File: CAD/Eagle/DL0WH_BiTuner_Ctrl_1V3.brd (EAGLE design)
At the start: 96.5 x 73 mm, 157 parts, among them Q0321 ABS07-32.768KHZ, U0101 STM32L476RGT6_64PIN_LDO, U0601 MC33996, U0701 MC33996, U0801 MC33996, U0921 TS5A23166, U0941 LM2611, U0951 OPA354, U0961 OPA354, U0962 MCP4661-103E-MS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

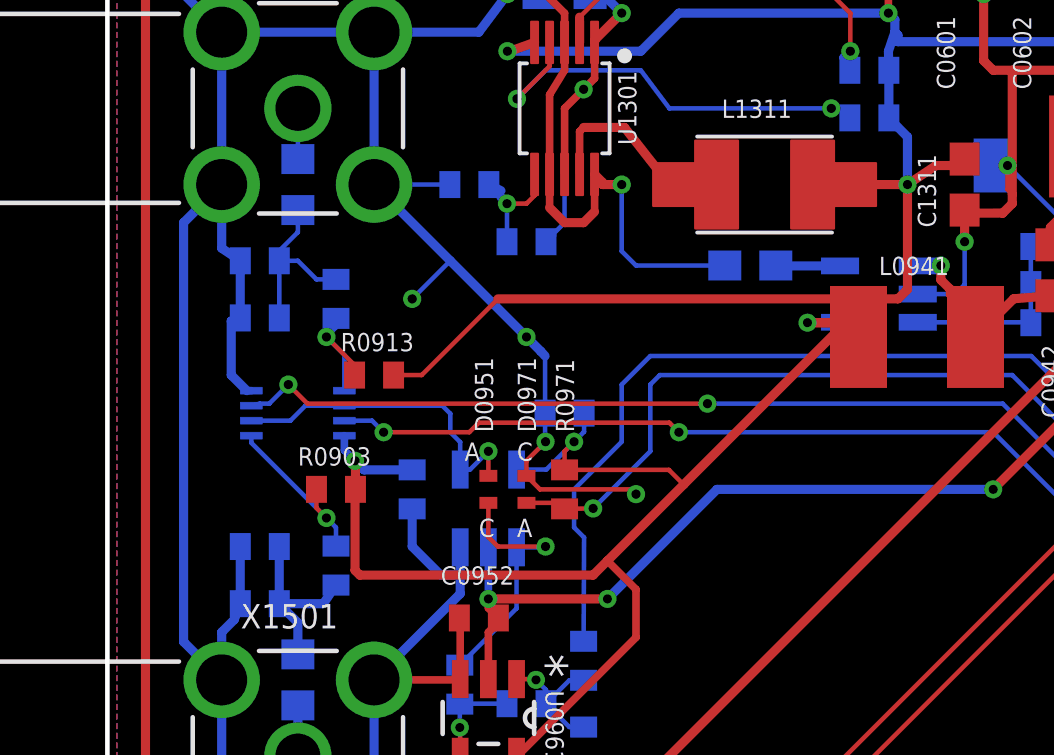
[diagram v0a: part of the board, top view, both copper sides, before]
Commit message: HW_1V3 - CAD/Eagle - minor fixes for measurement unit to work
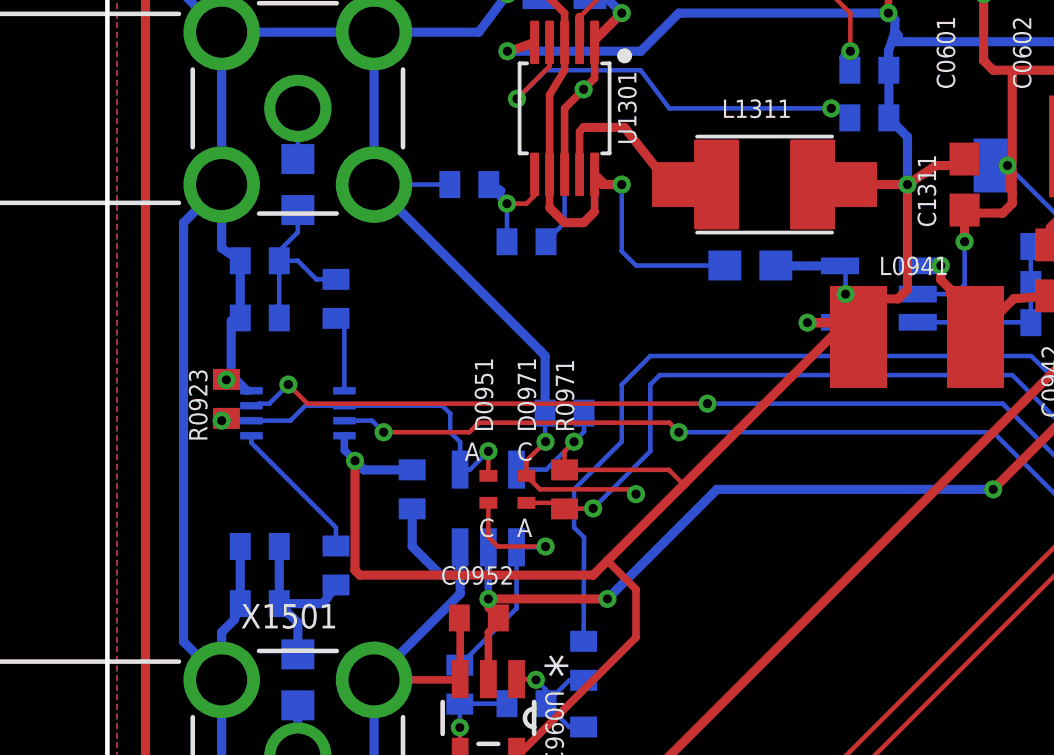
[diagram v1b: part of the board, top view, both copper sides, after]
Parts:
- removed R0903, R0913: 150kR, df4iah_rcl:R0402
- added R0923: 2MR, df4iah_rcl:R0402
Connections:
- net +3V3: no longer R0903.2, R0913.2
- net GND: now also R0923.1
- net SWR_IN_FWD: no longer R0903.1
- net SWR_IN_REV: no longer R0913.1
- net SWR_SEL_PWR: now also R0923.2
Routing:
- net +3V3: track 237.8 -> 223.0 mm, vias 11 -> 12
- net SWR_IN_REV: track 4.45 -> 2.53 mm, vias 1 -> 0
- net GND: track 904.0 -> 902.4 mm, vias 38 -> 37
- net SWR_SEL_PWR: track 11.0 -> 12.1 mm, vias 1 -> 2
- net SWR_IN_FWD: track 5.94 -> 4.85 mm, vias 1 -> 0
